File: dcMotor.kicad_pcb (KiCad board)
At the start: 2 copper layers, 145.7 x 97 mm, 88 parts, among them J1 Phoenix Contact 1803426, J2 Conn_01x06_Pin, J3 USB_C_Receptacle_USB2.0_16P, J4 Conn_Staubli_SLB4-F6,3-rot, J5 Conn_Staubli_SLB4-F6,3, J6 Conn_ST_STDC14, Q2 AO3400A, Q4 MMBT5401, Q5 MMBT5401, SW3 SW_Push, SW4 SW_Push, U1 NCP718xSN330, U10 STM32G431RBTx, U4 DRV8231ADDA, U5 MCP6561-OT, U7 ER_OLEDM0.91_1x-I2C, U8 LMR54406DBVR, U9 LTH-301-05

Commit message: Wip
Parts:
- removed C12: 1u, Capacitor_SMD:C_0603_1608Metric_Pad1.08x0.95mm_HandSolder
- removed REF**: na, PZ:na
- added C33: 1u, Capacitor_SMD:C_0402_1005Metric, F.Cu at (69.1, 88.4)
- C11: footprint Capacitor_SMD:C_0603_1608Metric_Pad1.08x0.95mm_HandSolder -> Capacitor_SMD:C_0402_1005Metric
- moved D6 142.6 mm to (76.7, 119.1), turned to 180 degrees
- moved D7 142.6 mm to (76.7, 114.0), turned to 180 degrees
- moved J6 7.76 mm to (59.2, 111.6), turned to -90 degrees
- moved FB1 5.00 mm to (69.3, 89.7), turned to 0 degrees
- moved C11 3.81 mm to (71.2, 91.4), turned to 0 degrees
- moved C30 0.25 mm to (68.6, 91.4)
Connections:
- C11 pad 1: GND -> Net-(U10-VREF+)
- C11 pad 2: Net-(U10-VREF+) -> GND
- J1 pad 1: /VEXT -> unconnected-(J1-Pin_1-Pad1)
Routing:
- net +3.3V: track 13.8 -> 19.8 mm
- net GND: track 45.7 -> 51.0 mm, vias 23 -> 25
- net Net-(U10-VREF+): track 2.50 -> 4.03 mm
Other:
- board text added: "TODO: Bohrungen am Rand Bohrungen für Motorhalterung"

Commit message: Wip
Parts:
- removed C15: 10n, Capacitor_SMD:C_0603_1608Metric
- removed C3: 1u, Capacitor_SMD:C_0603_1608Metric_Pad1.08x0.95mm_HandSolder
- removed C8: 100n, Capacitor_SMD:C_0805_2012Metric_Pad1.18x1.45mm_HandSolder
- removed D3: red, LED_SMD:LED_0603_1608Metric
- removed D9: KT-0805G, LED_SMD:LED_0805_2012Metric
- removed J1: Phoenix Contact 1803426, Connector_Phoenix_MC:PhoenixContact_MCV_1,5_2-G-3.81_1x02_P3.81mm_Vertical
- removed J2: Conn_01x06_Pin, Connector_PinHeader_2.54mm:PinHeader_1x06_P2.54mm_Vertical_SMD_Pin1Right
- removed Q4, Q5: MMBT5401, Package_TO_SOT_SMD:SOT-23_Handsoldering
- removed R13: 4.7k, Resistor_SMD:R_0603_1608Metric_Pad0.98x0.95mm_HandSolder
- removed R14, R15, R17: ~, Resistor_SMD:R_0805_2012Metric_Pad1.20x1.40mm_HandSolder
- removed R16: 470, Resistor_SMD:R_0603_1608Metric_Pad0.98x0.95mm_HandSolder
- removed R18, R19: 10k, Resistor_SMD:R_0805_2012Metric
- removed R23, R24, R25: 1k, Resistor_SMD:R_0805_2012Metric
- removed RV3, RV4: PTV09A-1020F-B203, PZ:Potentiometer_Bourns_PTV09A-1_Single_Vertical
- removed TP3: TP_Keystone_5095, PZ:TP_Keystone_5010-5014_Multipurpose
- removed TP9: TestPoint, PZ:TP_Keystone_5010-5014_Multipurpose
- added C7: 1u, Capacitor_SMD:C_0603_1608Metric_Pad1.08x0.95mm_HandSolder, F.Cu at (216.0, 137.8)
- moved U1 215.8 mm to (220.7, 136.4)
- moved C1 207.9 mm to (216.0, 135.3), turned to 0 degrees
- moved TP15 53.2 mm to (69.6, 70.0)

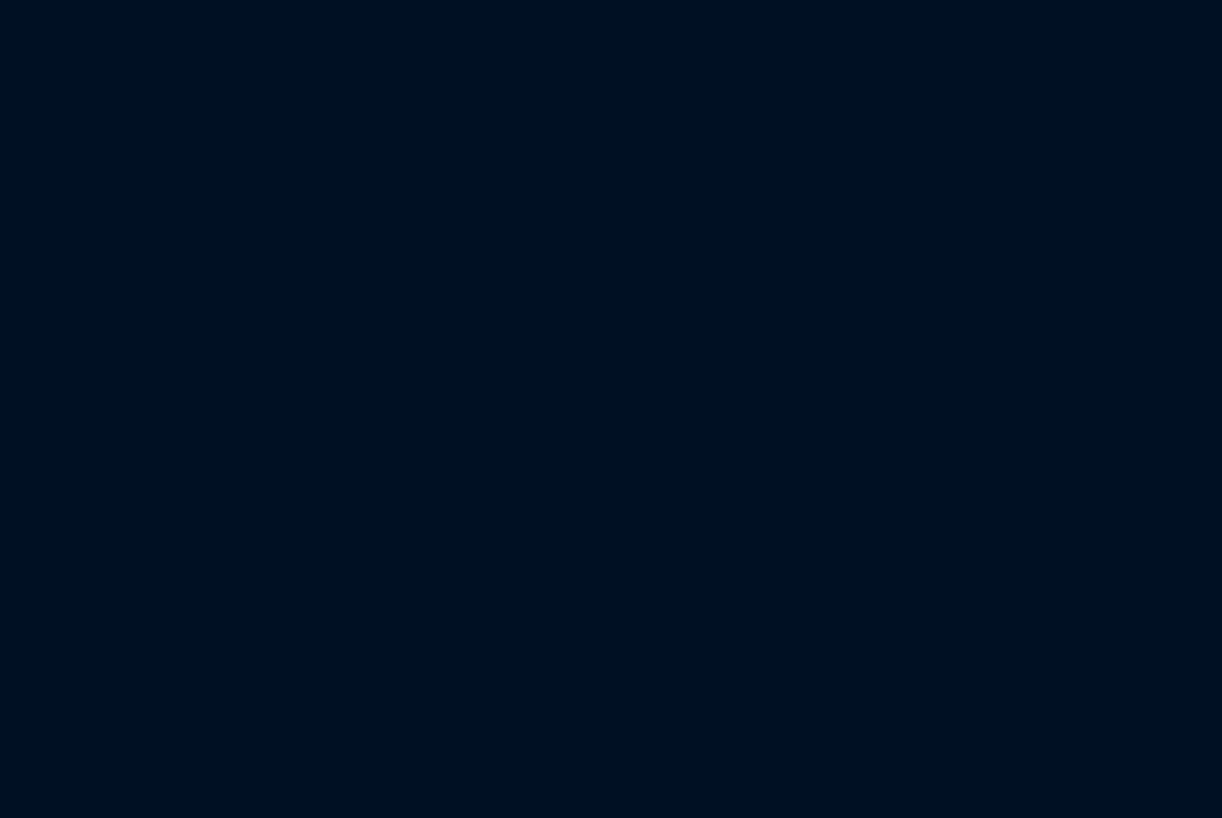
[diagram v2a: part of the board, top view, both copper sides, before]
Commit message: relocated dummy cad model
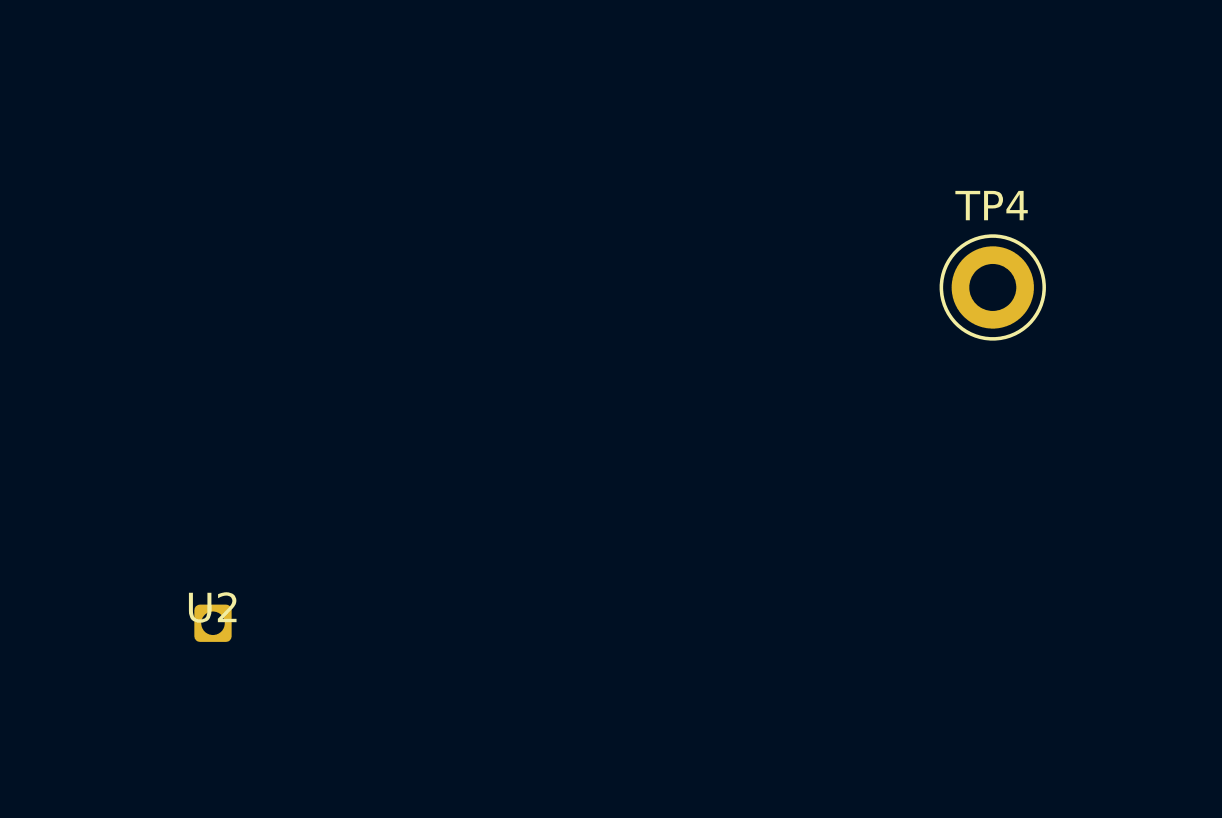
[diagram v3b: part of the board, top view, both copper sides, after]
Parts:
- added TP4: TP_Keystone_5095, PZ:TP_Keystone_5010-5014_Multipurpose, F.Cu at (137.8, 104.9)
- added U2: ~, PZ:na, F.Cu at (111.3, 116.3)

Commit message: Wip
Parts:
- moved U9 51.1 mm to (103.6, 129.3), turned to -90 degrees
- moved U2 29.8 mm to (105.2, 87.1), turned to -90 degrees
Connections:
- net /IN1 renamed /DRV_PWM_IN1
- net /IN2 renamed /DRV_PWM_IN2
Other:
- board text removed: "on/off"
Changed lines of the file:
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@@
 			(at 0 -2.4 90)
 			(layer "F.SilkS")
+			(hide yes)
 			(effects
 				(font
@@
 			(at 0 -1.68 0)
 			(layer "F.SilkS")
+			(hide yes)
 			(effects
 				(font
@@
 			(at 0 -3 0)
 			(layer "F.SilkS")
+			(hide yes)
 			(effects
 				(font
@@
 			(layer "F.Fab")
 		)
-		(fp_text user "${REFERENCE}"
-			(at 0 -3 0)
-			(layer "F.Fab")
-			(effects
-				(font
-					(size 1 1)
-					(thickness 0.15)
-				)
-			)
-		)
 		(pad "1" smd roundrect
 			(at -2.15 0 180)
@@
 			(at 0 2.75 0)
 			(layer "F.Fab")
+			(hide yes)
 			(effects
 				(font
@@
 				(name "A")
 				(pins "28" "7" "5" "6" "55" "8" "9" "10" "11" "22" "23" "38" "39" "40"
-					"41" "52" "53" "54" "2" "3" "4" "1" "16" "32" "31" "63" "15" "47" "48"
+					"41" "52" "53" "54" "2" "3" "4" "1" "16" "32" "47" "15" "63" "31" "48"
 					"27" "64" "29" "12" "13" "14" "17" "18" "19" "20" "21" "42" "43" "44"
 					"45" "46" "49" "50" "51" "24" "25" "26" "56" "57" "58" "59" "60" "61"
@@
 			(at 0 -1.16 0)
 			(layer "F.SilkS")
+			(hide yes)
 			(effects
 				(font
@@
 	(footprint "PZ:na"
 		(layer "F.Cu")
-		(at 111.252 116.332)
+		(at 105.223 87.122 -90)
 		(property "Reference" "U2"
-			(at 0 -0.5 0)
+			(at 0 -0.5 270)
 			(unlocked yes)
 			(layer "F.SilkS")
@@
 		)
 		(property "Value" "~"
-			(at 0 1 0)
+			(at 0 1 270)
 			(unlocked yes)
 			(layer "F.Fab")
@@
 		)
 		(property "Datasheet" ""
-			(at 0 0 0)
+			(at 0 0 270)
 			(unlocked yes)
 			(layer "F.Fab")
@@
 		)
 		(property "Description" "dummy 3D model"
-			(at 0 0 0)
+			(at 0 0 270)
 			(unlocked yes)
 			(layer "F.Fab")
@@
 		(duplicate_pad_numbers_are_jumpers no)
 		(fp_text user "${REFERENCE}"
-			(at 0 2.5 0)
+			(at 0 2.5 270)
 			(unlocked yes)
 			(layer "F.Fab")
@@
 		)
 		(pad "" np_thru_hole roundrect
-			(at 0 0)
+			(at 0 0 270)
 			(size 1.27 1.27)
 			(drill 0.8)
@@
 			(at 0 -3 0)
 			(layer "F.SilkS")
+			(hide yes)
 			(effects
 				(font
@@
 			(layer "F.Fab")
 		)
-		(fp_text user "${REFERENCE}"
-			(at 0 -3 0)
-			(layer "F.Fab")
-			(effects
-				(font
-					(size 1 1)
-					(thickness 0.15)
-				)
-			)
-		)
 		(pad "1" smd roundrect
 			(at -2.15 0 180)
@@
 			(at 0 -3.5 0)
 			(layer "F.SilkS")
+			(hide yes)
 			(effects
 				(font
@@
 			(size 2.2 0.5)
 			(layers "F.Cu" "F.Mask" "F.Paste")
-			(net "/IN2")
+			(net "/DRV_PWM_IN2")
 			(pinfunction "IN2_2")
 			(pintype "input")
@@
 			(size 2.2 0.5)
 			(layers "F.Cu" "F.Mask" "F.Paste")
-			(net "/IN1")
+			(net "/DRV_PWM_IN1")
 			(pinfunction "IN1_3")
 			(pintype "input")
@@
 	(footprint "PZ:LTH-301-05"
 		(layer "F.Cu")
-		(at 153.416 117.923)
+		(at 103.632 129.286 -90)
 		(property "Reference" "U9"
-			(at 0 -0.5 0)
+			(at 0 -0.5 270)
 			(unlocked yes)
 			(layer "F.SilkS")
@@
 		)
 		(property "Value" "LTH-301-05"
-			(at 0 1 0)
+			(at 0 1 270)
 			(unlocked yes)
 			(layer "F.Fab")
@@
 		)
 		(property "Datasheet" "https://optoelectronics.liteon.com/upload/download/DS-55-92-0002/H301-05.pdf"
-			(at 0 0 0)
+			(at 0 0 270)
 			(unlocked yes)
 			(layer "F.Fab")
@@
 		)
 		(property "Description" "Photointerruptor, Transmissive, 6mm"
-			(at 0 0 0)
+			(at 0 0 270)
 			(unlocked yes)
 			(layer "F.Fab")
@@
 		)
 		(property "LCSC Part #" "C575483"
-			(at 0 0 0)
+			(at 0 0 270)
 			(unlocked yes)
 			(layer "F.Fab")
@@
 		)
 		(property "Package" ""
-			(at 0 0 0)
+			(at 0 0 270)
 			(unlocked yes)
 			(layer "F.Fab")
@@
 		)
 		(pad "" np_thru_hole circle
-			(at -6.45 2.6)
+			(at -6.45 2.6 270)
 			(size 0.8 0.8)
 			(drill 0.8)
@@
 		)
 		(pad "" np_thru_hole circle
-			(at 2.15 -2.6)
+			(at 2.15 -2.6 270)
 			(size 0.8 0.8)
 			(drill 0.8)
@@
 		)
 		(pad "A" thru_hole circle
-			(at -5.225 -1.27 90)
+			(at -5.225 -1.27)
 			(size 1.25 1.25)
 			(drill 0.8)
@@
 		)
 		(pad "C" thru_hole circle
-			(at 5.225 -1.27 90)
+			(at 5.225 -1.27)
 			(size 1.25 1.25)
 			(drill 0.8)
@@
 		)
 		(pad "E" thru_hole circle
-			(at 5.225 1.27 90)
+			(at 5.225 1.27)
 			(size 1.25 1.25)
 			(drill 0.8)
@@
 		)
 		(pad "K" thru_hole circle
-			(at -5.225 1.27 90)
+			(at -5.225 1.27)
 			(size 1.25 1.25)
 			(drill 0.8)
@@
 			(at 0 -2.38 0)
 			(layer "F.SilkS")
+			(hide yes)
 			(effects
 				(font
@@
 			(at 0 -2.4 0)
 			(layer "F.SilkS")
+			(hide yes)
 			(effects
 				(font
@@
 			(at 0 -1.65 90)
 			(layer "F.SilkS")
+			(hide yes)
 			(effects
 				(font
@@
 			(at 0 -1.65 0)
 			(layer "F.SilkS")
+			(hide yes)
 			(effects
 				(font
@@
 			(layer "F.Fab")
 		)
-		(fp_text user "${REFERENCE}"
-			(at 0 0 0)
-			(layer "F.Fab")
-			(effects
-				(font
-					(size 0.5 0.5)
-					(thickness 0.08)
-				)
-			)
-		)
 		(pad "1" smd roundrect
 			(at -0.9125 0 180)
@@
 			(layers "*.Cu" "*.Mask")
 			(remove_unused_layers no)
-			(net "/IN1")
+			(net "/DRV_PWM_IN1")
 			(pinfunction "1_1")
 			(pintype "passive")
@@
 			(at 0 -1.16 0)
 			(layer "F.SilkS")
+			(hide yes)
 			(effects
 				(font
@@
 			(at 0 -1.65 90)
 			(layer "F.SilkS")
+			(hide yes)
 			(effects
 				(font
@@
 			(at 0.635 -1.745 90)
 			(layer "F.SilkS")
+			(hide yes)
 			(effects
 				(font
@@
 			(unit
 				(name "A")
-				(pins "S1" "A1" "A12" "B1" "B12" "A4" "A9" "B4" "B9" "A5" "B5" "A7" "B7"
+				(pins "S1" "B1" "B12" "A1" "A12" "A9" "B4" "B9" "A4" "A5" "B5" "A7" "B7"
 					"A6" "B6" "A8" "B8"
 				)
@@
 			(at 0 -1.68 0)
 			(layer "F.SilkS")
+			(hide yes)
 			(effects
 				(font
@@
 			(at 0 -1.16 90)
 			(layer "F.SilkS")
+			(hide yes)
 			(effects
 				(font
@@
 			(layers "*.Cu" "*.Mask")
 			(remove_unused_layers no)
-			(net "/IN2")
+			(net "/DRV_PWM_IN2")
 			(pinfunction "1_1")
 			(pintype "passive")
@@
 			(at 0 -1.16 0)
 			(layer "F.SilkS")
+			(hide yes)
 			(effects
 				(font
@@
 			(at 0 1.16 0)
 			(layer "F.Fab")
+			(hide yes)
 			(effects
 				(font
@@
 			(at 24.4475 -15.308241 0)
 			(layer "F.SilkS")
+			(hide yes)
 			(effects
 				(font
@@
 			(layer "F.Fab")
 		)
-		(fp_text user "${REFERENCE}"
-			(at 24.4475 -15.308241 0)
-			(layer "F.Fab")
-			(effects
-				(font
-					(size 1 1)
-					(thickness 0.15)
-				)
-			)
-		)
 		(pad "1" smd roundrect
 			(at -2 0)
@@
 			(at 0 -1.16 0)
 			(layer "F.SilkS")
+			(hide yes)
 			(effects
 				(font
@@
 				(bold yes)
 			)
-			(justify left bottom)
-		)
-	)
-	(gr_text "on/off"
-		(at 40.64 79.248 0)
-		(layer "F.SilkS")
-		(effects
-			(font
-				(size 1.1 1.1)
-				(thickness 0.18)
-				(bold yes)
-			)

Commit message: Wip
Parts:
- removed R28, R29: 1k, Resistor_SMD:R_0805_2012Metric
- added R30: 10k, Resistor_SMD:R_0805_2012Metric, F.Cu at (158.0, 118.7)
- added R31: 10k, Resistor_SMD:R_0805_2012Metric, F.Cu at (158.0, 121.7)
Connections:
- RV5 pad 1: Net-(R28-Pad2) -> unconnected-(RV5-Pad1)
- RV5 pad 3: Net-(R29-Pad1) -> unconnected-(RV5-Pad3)
- U5 pad 3: unconnected-(U5-+-Pad3) -> Net-(U5-+)
- U5 pad 4: unconnected-(U5---Pad4) -> /PHOTO_OUT

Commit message: wip
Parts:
- removed C1, C7: 1u, Capacitor_SMD:C_0603_1608Metric_Pad1.08x0.95mm_HandSolder
- removed U1: NCP718xSN330, Package_TO_SOT_SMD:SOT-23-5
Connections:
- RV5 pad MP: (no net) -> unconnected-(RV5-PadMP)

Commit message: wip
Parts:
- removed D6, D7: B240, Diode_SMD:D_SMB
- removed J4: Conn_Staubli_SLB4-F6,3-rot, PZ:Staubli_SLB4-F6,3-rot
- removed J5: Conn_Staubli_SLB4-F6,3, PZ:Staubli_SLB4-F6,3-schwarz
- added D3: SS54, Diode_SMD:D_SMA_Handsoldering, F.Cu at (53.8, 108.6)
- added J7: USB_C_Receptacle_USB2.0_16P, Connector_USB:USB_C_Receptacle_HCTL_HC-TYPE-C-16P-01A, F.Cu at (51.4, 116.1)
- moved SW3 171.7 mm to (70.0, 140.1)
- moved SW4 161.0 mm to (69.6, 130.6)
- moved C14 118.2 mm to (126.0, 138.0)
- moved C23 118.2 mm to (141.0, 137.0)
- moved R20 118.2 mm to (141.0, 133.0)
- moved R21 118.2 mm to (141.0, 135.0)
- moved C17 52.5 mm to (166.8, 136.7)
- moved TP1 52.5 mm to (167.9, 130.4)
- moved TP2 52.5 mm to (167.9, 135.5)
- moved RV5 52.5 mm to (167.0, 137.8)
- moved C18 26.6 mm to (187.2, 110.7)
- moved J6 13.5 mm to (72.6, 111.6)
- moved J3 9.14 mm to (51.5, 91.7)
- moved C5 9.14 mm to (58.8, 89.0)
- moved C6 9.14 mm to (59.0, 94.2)
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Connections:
- J3 pad A6: /USB_D+ -> unconnected-(J3-D+-PadA6)
- J3 pad A7: /USB_D- -> unconnected-(J3-D--PadA7)
- J3 pad B6: /USB_D+ -> unconnected-(J3-D+-PadB6)
- J3 pad B7: /USB_D- -> unconnected-(J3-D--PadB7)

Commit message: wip change to 48 pin package
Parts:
- removed C11, C33: 1u, Capacitor_SMD:C_0402_1005Metric
- removed C27, C28, C29, C30, C31: 100n, Capacitor_SMD:C_0402_1005Metric
- removed FB1: FerriteBead_Small, Resistor_SMD:R_0603_1608Metric_Pad0.98x0.95mm_HandSolder
- removed U10: STM32G431RBTx, Package_QFP:LQFP-64_10x10mm_P0.5mm
- added C12: 1u, Capacitor_SMD:C_0402_1005Metric, F.Cu at (62.7, 96.9)
- added C41: 100n, Capacitor_SMD:C_0402_1005Metric, F.Cu at (62.7, 98.9)
- added C42: 100n, Capacitor_SMD:C_0402_1005Metric, F.Cu at (62.7, 100.8)
- added C43: 100n, Capacitor_SMD:C_0402_1005Metric, F.Cu at (62.7, 102.8)
- added C44: 100n, Capacitor_SMD:C_0402_1005Metric, F.Cu at (62.7, 104.8)
- added C45: 1u, Capacitor_SMD:C_0402_1005Metric, F.Cu at (62.7, 106.8)
- added FB4: FerriteBead_Small, Resistor_SMD:R_0603_1608Metric_Pad0.98x0.95mm_HandSolder, F.Cu at (66.3, 108.5)
- added U6: STM32G431CBTx, Package_QFP:LQFP-48_7x7mm_P0.5mm, F.Cu at (69.8, 101.6)
- moved RV5 54.1 mm to (117.6, 115.8)
- moved J6 25.1 mm to (55.1, 129.5), turned to 0 degrees
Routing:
- net +3.3V: track 19.8 -> 11.8 mm
- net GND: track 51.0 -> 44.8 mm, vias 25 -> 22
- net Net-(U10-VREF+): track 4.03 -> 0.00 mm
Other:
- board text added: "DATA"
- board text added: "POWER"
